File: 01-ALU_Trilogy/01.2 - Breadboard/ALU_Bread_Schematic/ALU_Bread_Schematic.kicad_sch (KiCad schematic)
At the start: 3 parts

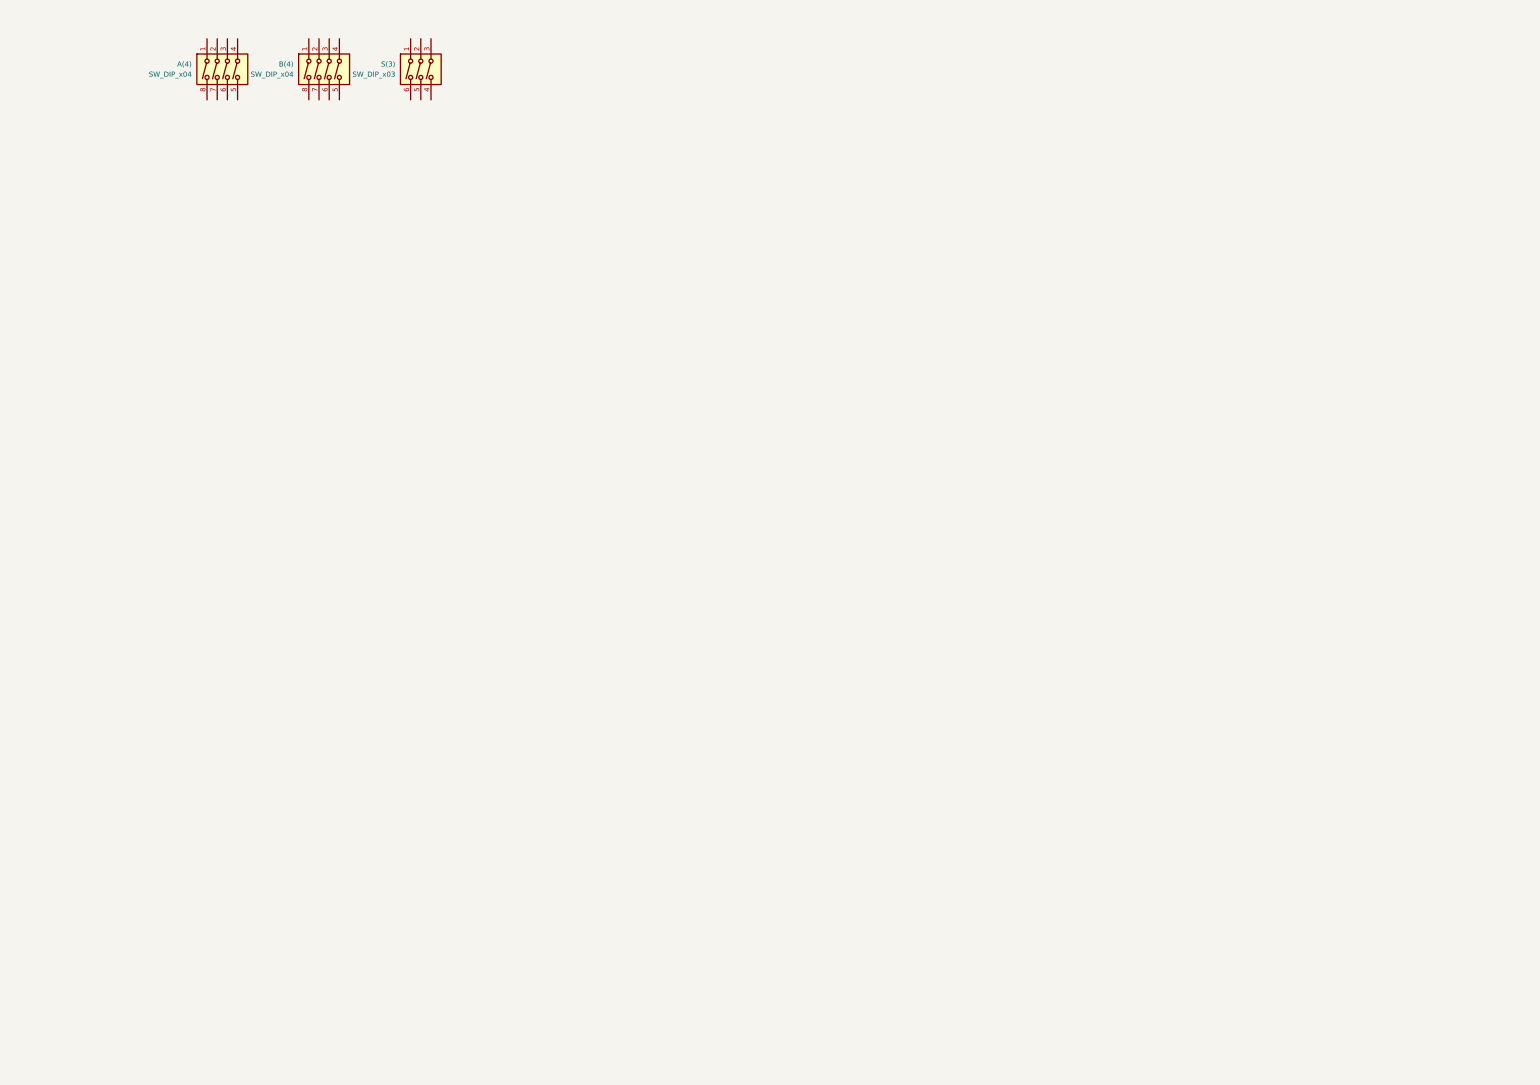
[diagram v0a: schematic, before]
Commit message: include first, flawed schematic
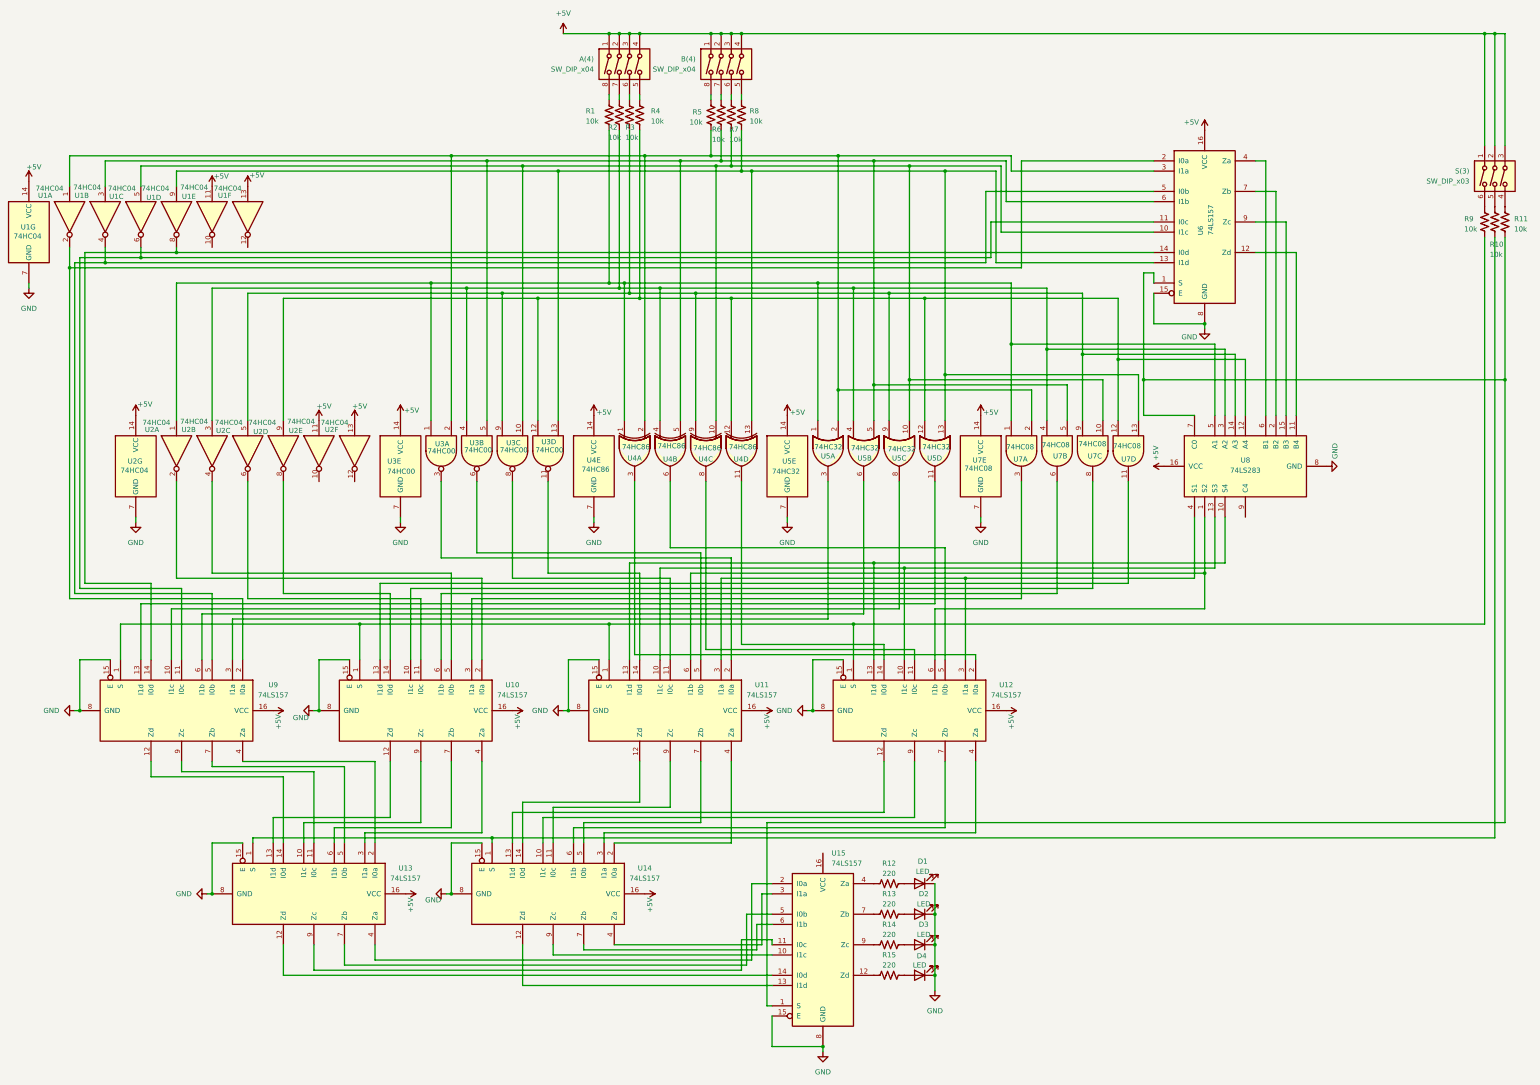
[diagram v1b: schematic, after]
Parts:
- added D1, D2, D3, D4: LED, symbol Device:LED
- added R1, R10, R11, R2, R3, R4, R5, R6, R7, R8, R9: 10k, symbol Device:R_US
- added R12, R13, R14, R15: 220, symbol Device:R_US
- added U1, U2: 74HC04, symbol 74xx:74HC04
- added U10, U11, U12, U13, U14, U15, U6, U9: 74LS157, symbol 74xx:74LS157
- added U3: 74HC00, symbol 74xx:74HC00
- added U4: 74HC86, symbol 74xx:74HC86
- added U5: 74HC32, symbol 74xx:74LS32
- added U7: 74HC08, symbol 74xx:74LS09
- added U8: 74LS283, symbol 74xx:74LS283
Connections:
- net +5V: now reaches A(4).1
- net +5V: now also A(4).2, A(4).3, A(4).4, B(4).1, B(4).2, B(4).3, B(4).4, S(3).1, S(3).2, S(3).3, U1.11, U1.13, U1.14 (VCC), U10.16 (VCC), U11.16 (VCC), U12.16 (VCC), U13.16 (VCC), U14.16 (VCC), U2.11, U2.13, U2.14 (VCC), U3.14 (VCC), U4.14 (VCC), U5.14 (VCC), U6.16 (VCC), U7.14 (VCC), U8.16 (VCC), U9.16 (VCC)
- net at A(4).5: now also R4.1
- net at A(4).6: now also R3.1
- net at A(4).7: now also R2.1
- net at A(4).8: now also R1.1
- net at S(3).4: now also R11.1
- net at S(3).5: now also R10.1
- net at S(3).6: now also R9.1
- net at B(4).5: now also R8.1
- net at B(4).6: now also R7.1
- net at B(4).7: now also R6.1
- net at B(4).8: now also R5.1
- new net: U1.8, U6.14 (I0d), U9.14 (I0d)
- new net: R8.2, U1.9, U3.13, U4.13, U5.13, U6.13 (I1d), U7.13
- new net: R10.2, U13.1 (S), U14.1 (S)
- new net: U10.9 (Zc), U13.10 (I1c)
- new net: U13.11 (I0c), U9.9 (Zc)
- new net: U13.12 (Zd), U15.14 (I0d)
- new net: U10.12 (Zd), U13.13 (I1d)
- new net: U13.14 (I0d), U9.12 (Zd)
- new net: U13.2 (I0a), U9.4 (Za)
- new net: U10.4 (Za), U13.3 (I1a)
- new net: U13.4 (Za), U15.2 (I0a)
- new net: U13.5 (I0b), U9.7 (Zb)
- new net: U10.7 (Zb), U13.6 (I1b)
- new net: U13.7 (Zb), U15.5 (I0b)
- new net: U13.9 (Zc), U15.11 (I0c)
- new net: R3.2, U2.5, U3.9, U4.9, U5.9, U7.9, U8.14 (A3)
- new net: R5.2, U1.1, U3.2, U4.2, U5.2, U6.3 (I1a), U7.2
- new net: U1.2, U6.2 (I0a), U9.2 (I0a)
- new net: R7.2, U1.5, U3.10, U4.10, U5.10, U6.10 (I1c), U7.10
- new net: U5.8, U9.10 (I1c)
- new net: R9.2, U10.1 (S), U11.1 (S), U12.1 (S), U9.1 (S)
- new net: U11.10 (I1c), U12.10 (I1c), U8.13 (S3)
- new net: U12.11 (I0c), U4.8
- new net: U12.12 (Zd), U14.13 (I1d)
- new net: U11.13 (I1d), U12.13 (I1d), U8.10 (S4)
- new net: U12.14 (I0d), U4.11
- new net: U12.2 (I0a), U4.3
- new net: U11.3 (I1a), U12.3 (I1a), U8.4 (S1)
- new net: U12.4 (Za), U14.3 (I1a)
- new net: U12.5 (I0b), U4.6
- new net: U11.6 (I1b), U12.6 (I1b), U8.1 (S2)
- new net: U12.7 (Zb), U14.6 (I1b)
- new net: U12.9 (Zc), U14.10 (I1c)
- new net: R4.2, U2.9, U3.12, U4.12, U5.12, U7.12, U8.12 (A4)
- new net: U11.11 (I0c), U3.8
- new net: R1.2, U2.1, U3.1, U4.1, U5.1, U7.1, U8.5 (A1)
- new net: U5.11, U9.13 (I1d)
- new net: U11.9 (Zc), U14.11 (I0c)
- new net: U14.12 (Zd), U15.13 (I1d)
- new net: U11.12 (Zd), U14.14 (I0d)
- new net: U11.4 (Za), U14.2 (I0a)
- new net: U14.4 (Za), U15.3 (I1a)
- new net: U11.7 (Zb), U14.5 (I0b)
- new net: U14.7 (Zb), U15.6 (I1b)
- new net: U14.9 (Zc), U15.10 (I1c)
- new net: R2.2, U2.3, U3.4, U4.4, U5.4, U7.4, U8.3 (A2)
- new net: R6.2, U1.3, U3.5, U4.5, U5.5, U6.6 (I1b), U7.5
- new net: U11.5 (I0b), U3.6
- new net: U10.14 (I0d), U2.8
- new net: D1.2 (A), R12.2
- new net: U5.6, U9.6 (I1b)
- new net: U10.10 (I1c), U7.8
- new net: U10.11 (I0c), U2.6
- new net: U10.13 (I1d), U7.11
- new net: U10.2 (I0a), U2.2
- new net: U10.3 (I1a), U7.3
- new net: U10.5 (I0b), U2.4
- new net: U10.6 (I1b), U7.6
- new net: U1.6, U6.11 (I0c), U9.11 (I0c)
- new net: U5.3, U9.3 (I1a)
- new net: U1.4, U6.5 (I0b), U9.5 (I0b)
- new net: U11.14 (I0d), U3.11
- new net: U11.2 (I0a), U3.3
- new net: R11.2, U15.1 (S), U6.1 (S), U8.7 (C0)
- new net: D3.2 (A), R14.2
- new net: D4.2 (A), R15.2
- new net: U6.12 (Zd), U8.11 (B4)
- new net: U6.9 (Zc), U8.15 (B3)
- new net: U6.7 (Zb), U8.2 (B2)
- new net: U6.4 (Za), U8.6 (B1)
- new net: R15.1, U15.12 (Zd)
- new net: R12.1, U15.4 (Za)
- new net: R13.1, U15.7 (Zb)
- new net: R14.1, U15.9 (Zc)
- new net: D2.2 (A), R13.2
- new net GND: D1.1 (K), D2.1 (K), D3.1 (K), D4.1 (K), U1.7 (GND), U10.15 (E), U10.8 (GND), U11.15 (E), U11.8 (GND), U12.15 (E), U12.8 (GND), U13.15 (E), U13.8 (GND), U14.15 (E), U14.8 (GND), U15.15 (E), U15.8 (GND), U2.7 (GND), U3.7 (GND), U4.7 (GND), U5.7 (GND), U6.15 (E), U6.8 (GND), U7.7 (GND), U8.8 (GND), U9.15 (E), U9.8 (GND)
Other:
- moved on the sheet: A(4), B(4), S(3)
